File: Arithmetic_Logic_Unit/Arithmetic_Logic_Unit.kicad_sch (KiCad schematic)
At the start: 1 part, among them J1 PC104

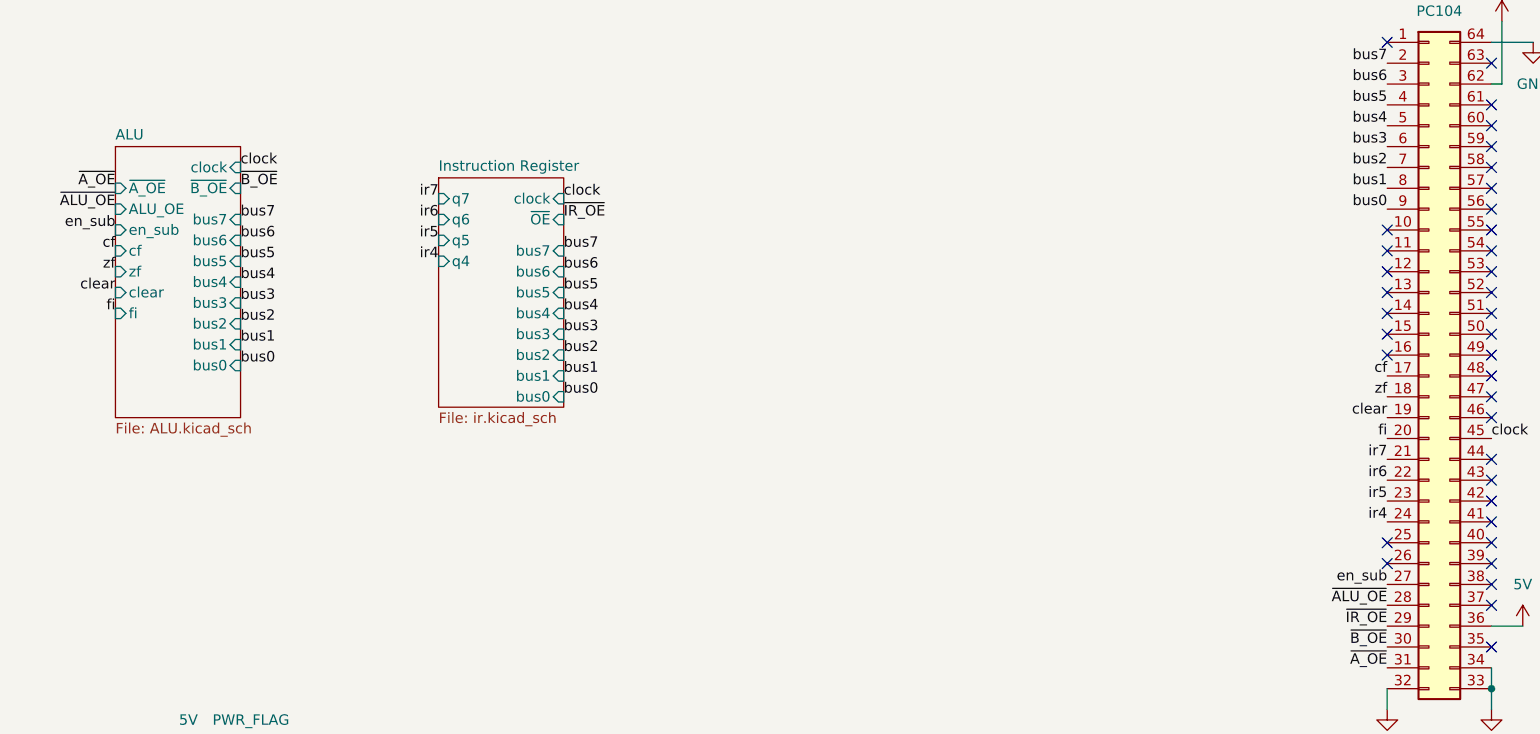
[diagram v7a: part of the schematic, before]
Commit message: fixed incorrect footprint for sn54173
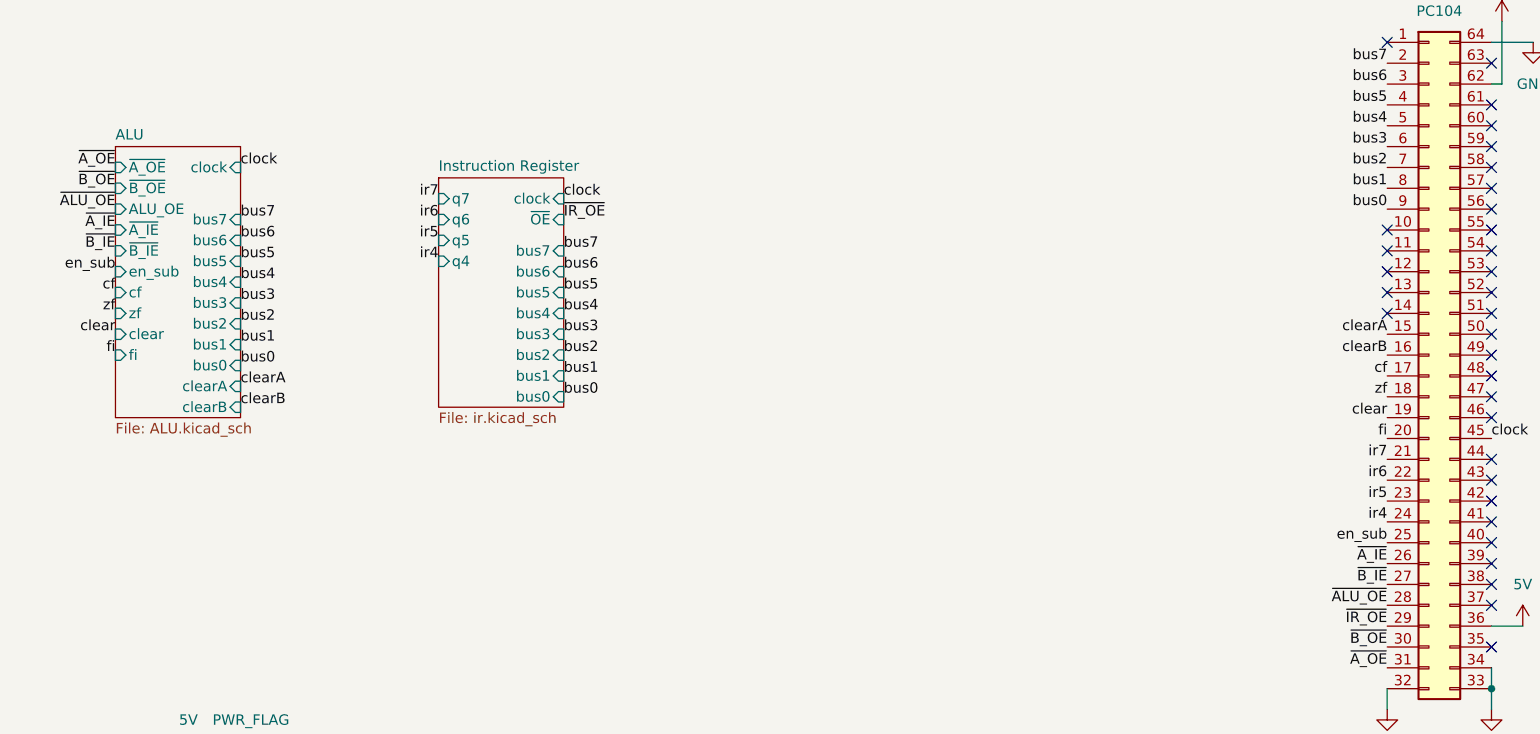
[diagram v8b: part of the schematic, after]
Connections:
- net en_sub: now also J1.25 (Pin_25); no longer J1.27 (Pin_27)
- net clearA: now reaches J1.15 (Pin_15)
- net clearB: now reaches J1.16 (Pin_16)
- net ~{A_IE}: now reaches J1.26 (Pin_26)
- new net ~{B_IE}: J1.27 (Pin_27)
- no-connect marks 36 -> 32
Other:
- sheet ALU ports: added clearA, clearB, ~{A_IE}, ~{B_IE}; removed none
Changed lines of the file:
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@@
-	)
-	(no_connect
-		(at 250.19 91.44)
 	)
 	(no_connect
@@
 	)
 	(no_connect
-		(at 250.19 88.9)
-	)
-	(no_connect
 		(at 250.19 53.34)
 	)
@@
 	)
 	(no_connect
-		(at 250.19 63.5)
-	)
-	(no_connect
 		(at 262.89 68.58)
 	)
@@
 	(no_connect
 		(at 262.89 58.42)
-	)
-	(no_connect
-		(at 250.19 66.04)
 	)
 	(no_connect
@@
 		)
 	)
+	(label "clearB"
+		(at 110.49 72.39 0)
+		(fields_autoplaced yes)
+		(effects
+			(font
+				(size 1.27 1.27)
+			)
+			(justify left bottom)
+		)
+	)
 	(label "bus6"
 		(at 250.19 33.02 180)
@@
 	)
 	(label "en_sub"
-		(at 95.25 50.8 180)
+		(at 95.25 55.88 180)
 		(fields_autoplaced yes)
 		(effects
@@
 	)
 	(label "cf"
-		(at 95.25 53.34 180)
+		(at 95.25 58.42 180)
 		(fields_autoplaced yes)
 		(effects
@@
 		)
 	)
+	(label "~{A_IE}"
+		(at 250.19 91.44 180)
+		(fields_autoplaced yes)
+		(effects
+			(font
+				(size 1.27 1.27)
+			)
+			(justify right bottom)
+		)
+	)
+	(label "~{B_IE}"
+		(at 250.19 93.98 180)
+		(fields_autoplaced yes)
+		(effects
+			(font
+				(size 1.27 1.27)
+			)
+			(justify right bottom)
+		)
+	)
+	(label "clearA"
+		(at 110.49 69.85 0)
+		(fields_autoplaced yes)
+		(effects
+			(font
+				(size 1.27 1.27)
+			)
+			(justify left bottom)
+		)
+	)
 	(label "clock"
 		(at 110.49 43.18 0)
@@
 		)
 	)
+	(label "clearB"
+		(at 250.19 66.04 180)
+		(fields_autoplaced yes)
+		(effects
+			(font
+				(size 1.27 1.27)
+			)
+			(justify right bottom)
+		)
+	)
 	(label "bus4"
 		(at 149.86 60.96 0)
@@
 		)
 	)
+	(label "clearA"
+		(at 250.19 63.5 180)
+		(fields_autoplaced yes)
+		(effects
+			(font
+				(size 1.27 1.27)
+			)
+			(justify right bottom)
+		)
+	)
 	(label "ir7"
 		(at 134.62 46.99 180)
@@
 	)
 	(label "fi"
-		(at 95.25 60.96 180)
+		(at 95.25 66.04 180)
 		(fields_autoplaced yes)
 		(effects
@@
 	)
 	(label "zf"
-		(at 95.25 55.88 180)
+		(at 95.25 60.96 180)
 		(fields_autoplaced yes)
 		(effects
@@
 		)
 	)
+	(label "~{A_IE}"
+		(at 95.25 50.8 180)
+		(fields_autoplaced yes)
+		(effects
+			(font
+				(size 1.27 1.27)
+			)
+			(justify right bottom)
+		)
+	)
 	(label "~{ALU_OE}"
 		(at 95.25 48.26 180)
@@
 		)
 	)
+	(label "~{B_IE}"
+		(at 95.25 53.34 180)
+		(fields_autoplaced yes)
+		(effects
+			(font
+				(size 1.27 1.27)
+			)
+			(justify right bottom)
+		)
+	)
 	(label "~{A_OE}"
-		(at 95.25 45.72 180)
+		(at 95.25 43.18 180)
 		(fields_autoplaced yes)
 		(effects
@@
 	)
 	(label "en_sub"
-		(at 250.19 93.98 180)
+		(at 250.19 88.9 180)
 		(fields_autoplaced yes)
 		(effects
@@
 	)
 	(label "~{B_OE}"
-		(at 110.49 45.72 0)
-		(fields_autoplaced yes)
-		(effects
-			(font
-				(size 1.27 1.27)
-			)
-			(justify left bottom)
+		(at 95.25 45.72 180)
+		(fields_autoplaced yes)
+		(effects
+			(font
+				(size 1.27 1.27)
+			)
+			(justify right bottom)
 		)
 	)
 	(label "clear"
-		(at 95.25 58.42 180)
+		(at 95.25 63.5 180)
 		(fields_autoplaced yes)
 		(effects
@@
 		(dnp no)
 		(fields_autoplaced yes)
-		(property "Reference" "#PWR044"
+		(property "Reference" "#PWR02"
 			(at 111.76 125.73 0)
 			(effects
@@
 			(project "Arithmetic_Logic_Unit"
 				(path "/71235e3f-9de8-4596-887a-1aa4526e80d1"
-					(reference "#PWR044")
+					(reference "#PWR02")
 					(unit 1)
 				)
@@
 		(dnp no)
 		(fields_autoplaced yes)
-		(property "Reference" "#PWR052"
+		(property "Reference" "#PWR04"
 			(at 262.89 115.57 0)
 			(effects
@@
 			(project "Arithmetic_Logic_Unit"
 				(path "/71235e3f-9de8-4596-887a-1aa4526e80d1"
-					(reference "#PWR052")
+					(reference "#PWR04")
 					(unit 1)
 				)
@@
 		(dnp no)
 		(fields_autoplaced yes)
-		(property "Reference" "#PWR055"
+		(property "Reference" "#PWR05"
 			(at 264.16 29.21 0)
 			(effects
@@
 			(project "Arithmetic_Logic_Unit"
 				(path "/71235e3f-9de8-4596-887a-1aa4526e80d1"
-					(reference "#PWR055")
+					(reference "#PWR05")
 					(unit 1)
 				)
@@
 		(dnp no)
 		(fields_autoplaced yes)
-		(property "Reference" "#PWR056"
+		(property "Reference" "#PWR06"
 			(at 266.7 102.87 0)
 			(effects
@@
 			(project "Arithmetic_Logic_Unit"
 				(path "/71235e3f-9de8-4596-887a-1aa4526e80d1"
-					(reference "#PWR056")
+					(reference "#PWR06")
 					(unit 1)
 				)
@@
 		(dnp no)
 		(fields_autoplaced yes)
-		(property "Reference" "#PWR043"
+		(property "Reference" "#PWR01"
 			(at 104.14 119.38 0)
 			(effects
@@
 			(project "Arithmetic_Logic_Unit"
 				(path "/71235e3f-9de8-4596-887a-1aa4526e80d1"
-					(reference "#PWR043")
+					(reference "#PWR01")
 					(unit 1)
 				)
@@
 		(dnp no)
 		(fields_autoplaced yes)
-		(property "Reference" "#PWR054"
+		(property "Reference" "#PWR07"
 			(at 267.97 34.29 0)
 			(effects
@@
 			(project "Arithmetic_Logic_Unit"
 				(path "/71235e3f-9de8-4596-887a-1aa4526e80d1"
-					(reference "#PWR054")
+					(reference "#PWR07")
 					(unit 1)
 				)
@@
 		(dnp no)
 		(fields_autoplaced yes)
-		(property "Reference" "#PWR053"
+		(property "Reference" "#PWR03"
 			(at 250.19 115.57 0)
 			(effects
@@
 			(project "Arithmetic_Logic_Unit"
 				(path "/71235e3f-9de8-4596-887a-1aa4526e80d1"
-					(reference "#PWR053")
+					(reference "#PWR03")
 					(unit 1)
 				)
@@
 		)
 		(pin "~{B_OE}" input
-			(at 110.49 45.72 0)
-			(effects
-				(font
-					(size 1.27 1.27)
-				)
-				(justify right)
+			(at 95.25 45.72 180)
+			(effects
+				(font
+					(size 1.27 1.27)
+				)
+				(justify left)
 			)
 		)
@@
 		)
 		(pin "~{A_OE}" input
-			(at 95.25 45.72 180)
+			(at 95.25 43.18 180)
 			(effects
 				(font
@@
 		)
 		(pin "en_sub" input
+			(at 95.25 55.88 180)
+			(effects
+				(font
+					(size 1.27 1.27)
+				)
+				(justify left)
+			)
+		)
+		(pin "fi" input
+			(at 95.25 66.04 180)
+			(effects
+				(font
+					(size 1.27 1.27)
+				)
+				(justify left)
+			)
+		)
+		(pin "clear" input
+			(at 95.25 63.5 180)
+			(effects
+				(font
+					(size 1.27 1.27)
+				)
+				(justify left)
+			)
+		)
+		(pin "zf" input
+			(at 95.25 60.96 180)
+			(effects
+				(font
+					(size 1.27 1.27)
+				)
+				(justify left)
+			)
+		)
+		(pin "cf" input
+			(at 95.25 58.42 180)
+			(effects
+				(font
+					(size 1.27 1.27)
+				)
+				(justify left)
+			)
+		)
+		(pin "~{A_IE}" input
 			(at 95.25 50.8 180)
 			(effects
@@
 			)
 		)
-		(pin "fi" input
-			(at 95.25 60.96 180)
-			(effects
-				(font
-					(size 1.27 1.27)
-				)
-				(justify left)
-			)
-		)
-		(pin "clear" input
-			(at 95.25 58.42 180)
-			(effects
-				(font
-					(size 1.27 1.27)
-				)
-				(justify left)
-			)
-		)
-		(pin "zf" input
-			(at 95.25 55.88 180)
-			(effects
-				(font
-					(size 1.27 1.27)
-				)
-				(justify left)
-			)
-		)
-		(pin "cf" input
+		(pin "clearA" input
+			(at 110.49 69.85 0)
+			(effects
+				(font
+					(size 1.27 1.27)
+				)
+				(justify right)
+			)
+		)
+		(pin "clearB" input
+			(at 110.49 72.39 0)
+			(effects
+				(font
+					(size 1.27 1.27)
+				)
+				(justify right)
+			)
+		)
+		(pin "~{B_IE}" input
 			(at 95.25 53.34 180)
 			(effects
